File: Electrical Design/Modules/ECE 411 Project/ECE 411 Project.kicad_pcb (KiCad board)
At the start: 2 copper layers, 87.8 x 99.9 mm, 141 parts, among them J1 5mm 9V Barrel, J2 BOOST, J3 Pheonix Connector, J4 1/8in Jack, J5 1x2 header, J6 1x2header, J7 1x2header, M4 MountingHole_4.3mm_M4_Pad_Top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, Q2 2N3904, Q3 2N3904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

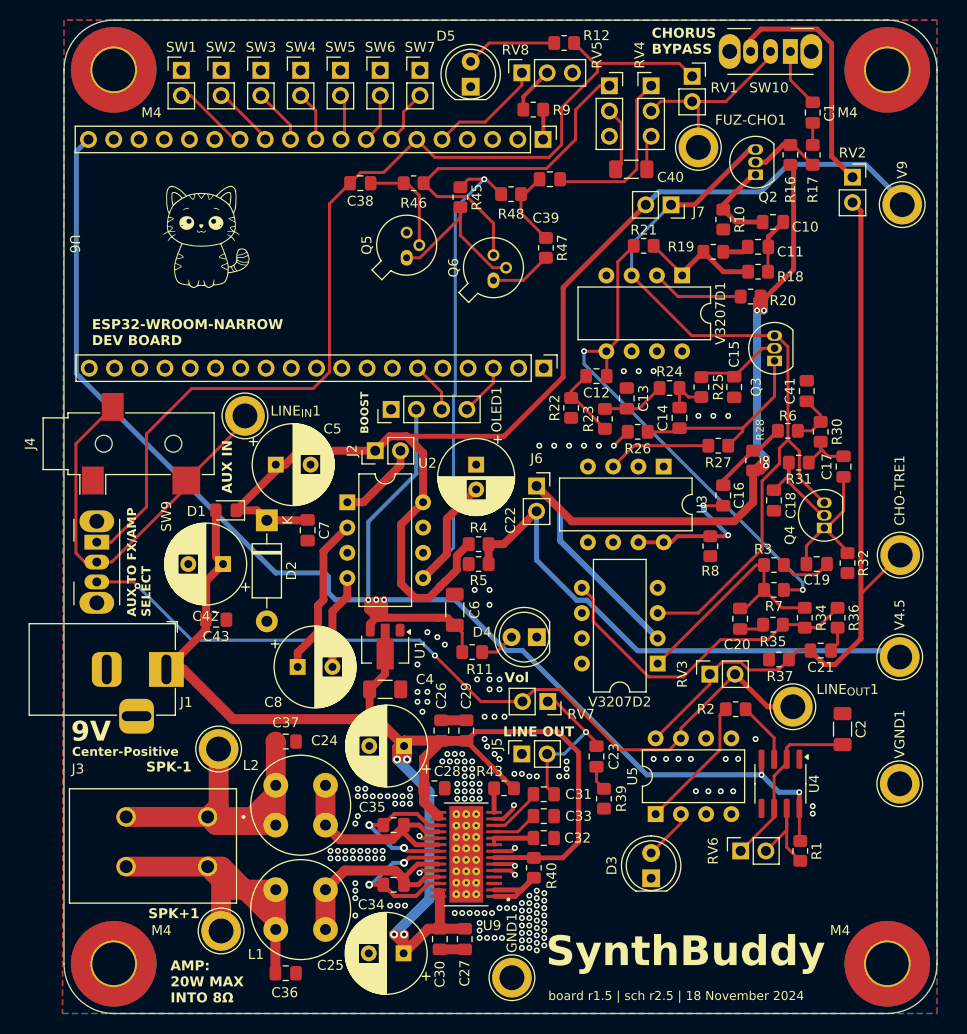
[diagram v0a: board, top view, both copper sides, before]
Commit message: adding chorus test poiunts, touch ups
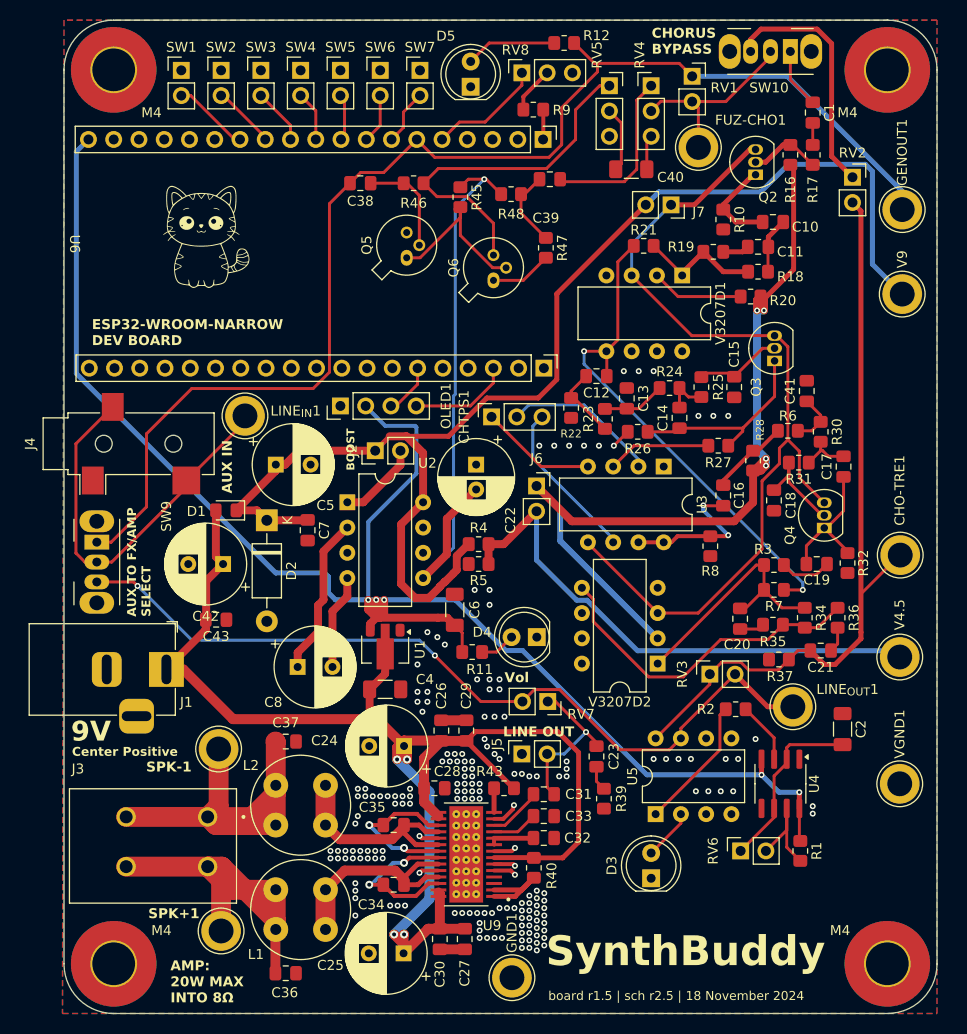
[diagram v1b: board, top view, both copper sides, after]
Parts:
- added CHTPS1: Conn_01x03_Pin, Connector_PinSocket_2.54mm:PinSocket_1x03_P2.54mm_Vertical, F.Cu at (74.7, 63.6)
- added GENOUT1: TestPoint, TestPoint:TestPoint_Loop_D3.80mm_Drill2.5mm, F.Cu at (116.0, 42.8)
- moved V9 9.00 mm to (116.0, 51.2)
- moved OLED1 5.11 mm to (59.5, 62.5)
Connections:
- U3 pad 2: unconnected-(U3-CP1-Pad2) -> Net-(CHTPS1-Pin_2)
- U3 pad 4: unconnected-(U3-VGG-Pad4) -> Net-(CHTPS1-Pin_1)
- U3 pad 5: /Chorus Effect/CLK -> /Chorus Effect/Vin
- U3 pad 6: unconnected-(U3-CP2-Pad6) -> Net-(CHTPS1-Pin_3)
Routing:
- net /FX: track 102.0 -> 129.7 mm
- net Net-(CHTPS1-Pin_3): track 0.00 -> 16.3 mm
- net Net-(CHTPS1-Pin_2): track 0.00 -> 15.7 mm
- net Net-(CHTPS1-Pin_1): track 0.00 -> 11.8 mm
- net +9V: track 123.4 -> 133.9 mm
- net /Chorus Effect/Vin: track 80.7 -> 90.7 mm
- net /SCL: track 5.25 -> 10.2 mm
- net +5V: track 161.6 -> 165.8 mm
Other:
- board text added: "Center Positive"
- board text removed: "Center-Positive"

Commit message: FINAL DESIGN PACKAGE
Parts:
- added G***: LOGO, LOGO, B.Cu at (40.0, 73.5)
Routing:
- net GND: vias 173 -> 403
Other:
- board text added: "1/4{dblquote} OUT"
- board text added: "Design: Eric Sanman Sierra Buckley Chris Crider Chuong Vo"
- board text added: "ECE411 Team 8 - The Voltage Vanguard board r1.6 | sch. r2.5 | 21 November 2024"
- board text added: "POWER"
- board text added: "TREMOLO CLOCK"
- board text added: "VOL"
- board text added: "WAVE"
- board text removed: "LINE OUT"
- board text removed: "Vol"
- board text removed: "board r1.5 | sch r2.5 | 18 November 2024"

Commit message: minor formatting updates
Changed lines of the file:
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@@
 		(tags "3.5mm audio cui horizontal jack stereo")
 		(property "Reference" "J4"
-			(at 0 -9.9 90)
+			(at 0 0 180)
 			(layer "F.SilkS")
 			(effects
